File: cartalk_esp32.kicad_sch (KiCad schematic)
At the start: 24 parts, among them IC1 CP2104, J1 10118192-0002LF, Q1 mmbt2222, Q2 mmbt2222, SW2 KMR2, U1 HUB75 Connector Female, U2 AP2112-3.3, X2 ESP32_WROOM32_SKINNY

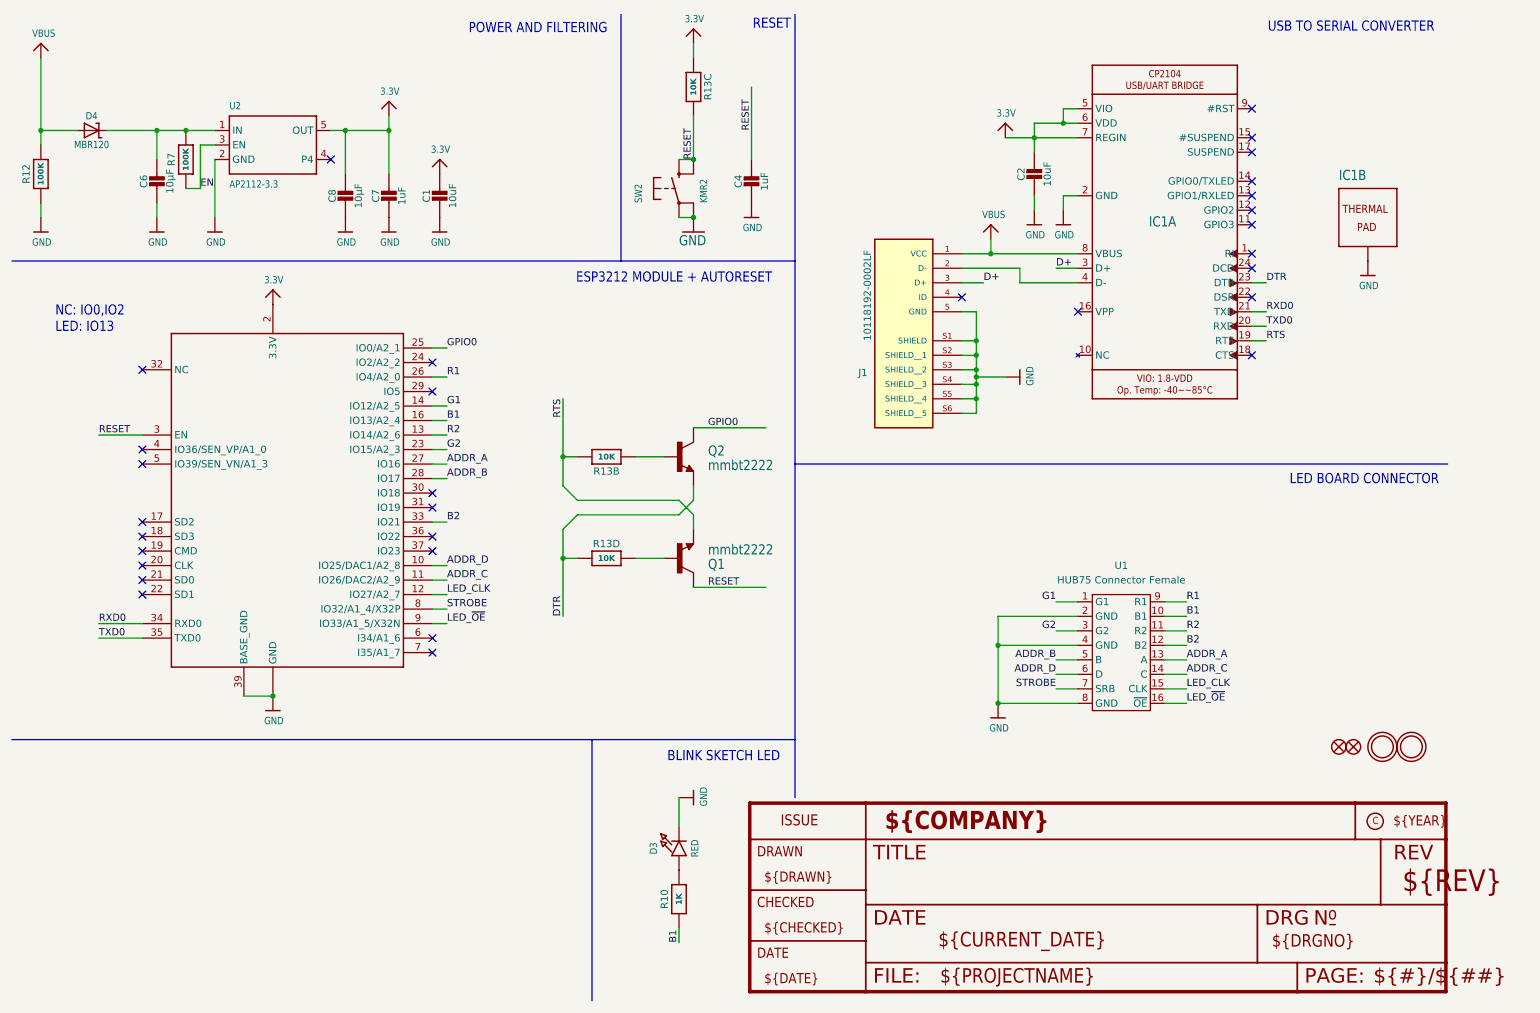
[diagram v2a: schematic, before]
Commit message: Fix remaining symbol-footprint pin mismatches.
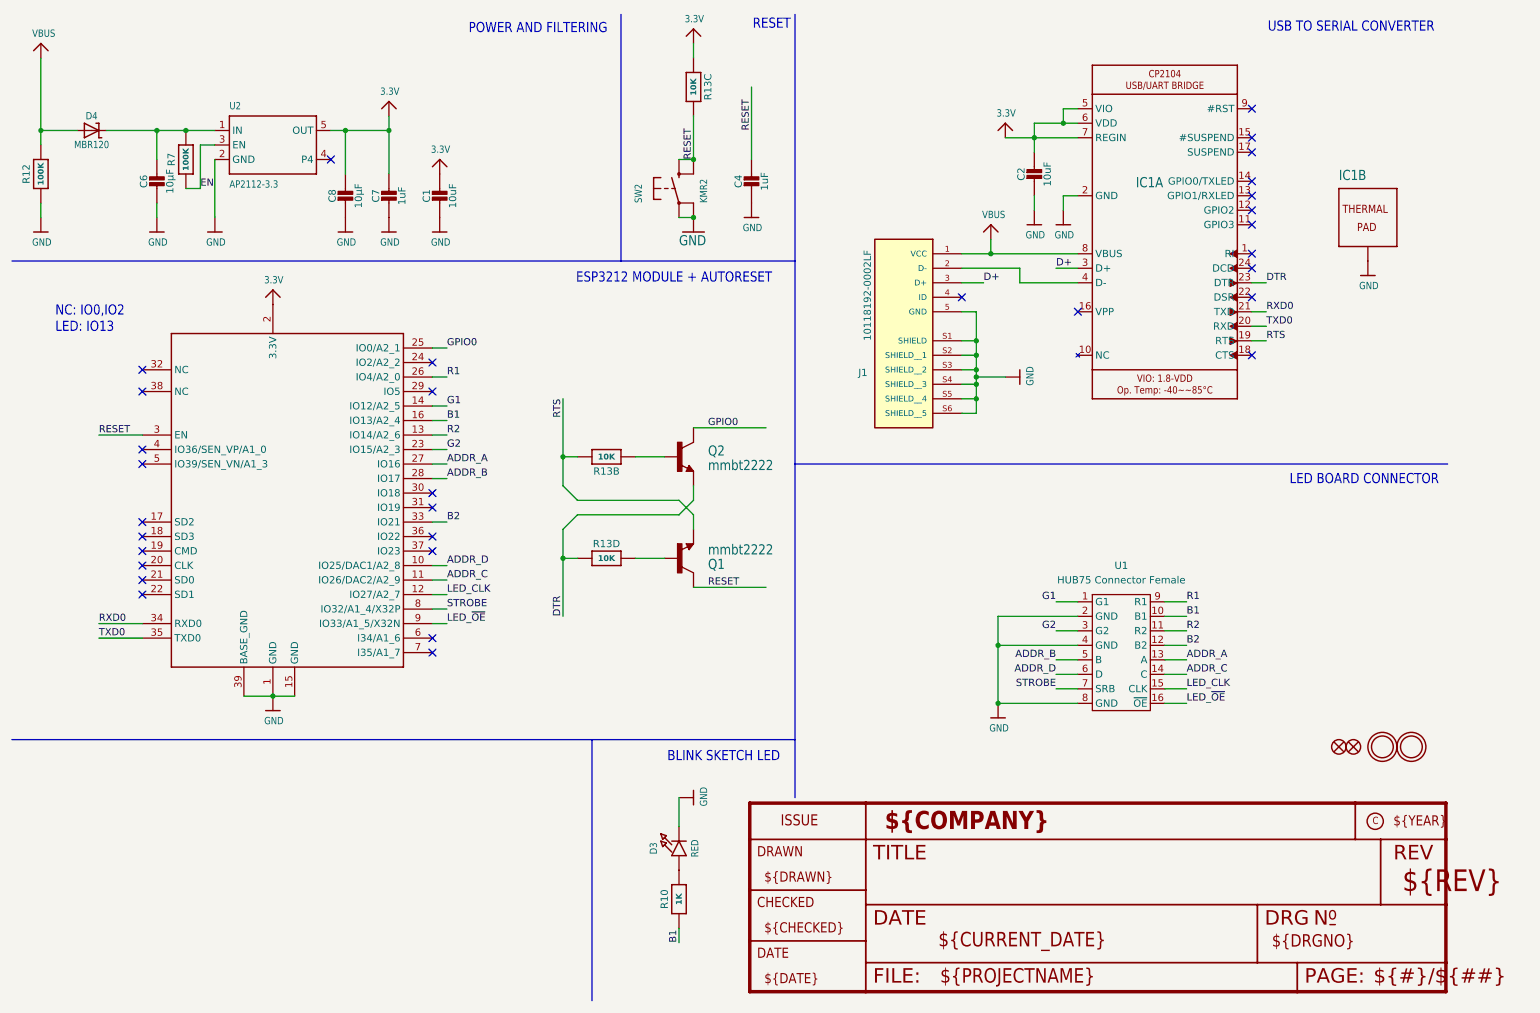
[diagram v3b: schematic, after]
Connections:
- net GND: now also D3.2 (C), IC1.25 (TP), SW2.1 (P), SW2.2 (P1); no longer D3.C, IC1.THERM (TP), SW2.A (P), SW2.A' (P1), X2.38 (GND), X2.P$1 (GND)
- net RESET: now also SW2.3 (S), SW2.4 (S1); no longer SW2.B (S), SW2.B' (S1)
- net VBUS: now also D4.1 (A); no longer D4.A
- net at C6.1, R7.2, U2.1 (IN): now also D4.2 (C); no longer D4.C
- net at R10.2: now also D3.1 (A); no longer D3.A
- no-connect marks 31 -> 32
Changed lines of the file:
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@@
 	)
 	(no_connect
+		(at 45.72 88.9)
+	)
+	(no_connect
 		(at 240.03 57.15)
 	)
@@
 		)
 	)
+	(wire
+		(pts
+			(xy 68.58 142.24) (xy 72.39 142.24)
+		)
+		(stroke
+			(width 0)
+			(type default)
+		)
+	)
 	(polyline
 		(pts
@@
 		(pin "9"
 		)
-		(pin "P$1"
-		)
 		(pin "18"
 		)
@@
 		(pin "37"
 		)
-		(pin "38"
-		)
 		(pin "4"
 		)
@@
 		(pin "14"
 		)
-		(pin "15"
-		)
 		(pin "16"
 		)
@@
 		(pin "32"
 		)
+		(pin "15"
+		)
+		(pin "38"
+		)
 		(instances
 			(project "cartalk_esp32"
@@
 	)
 	(symbol
+		(lib_name "CP2104_1")
 		(lib_id "cartalk_esp32-eagle-import:CP2104")
 		(at 224.79 59.69 0)
@@
 		(dnp no)
 		(property "Reference" "IC1"
-			(at 221.996 60.198 0)
+			(at 219.71 53.34 0)
 			(effects
 				(font
@@
 		(pin "9"
 		)
-		(pin "THERM"
+		(pin "25"
 		)
 		(instances
@@
 			)
 		)
-		(pin "C"
+		(pin "1"
 		)
-		(pin "A"
+		(pin "2"
 		)
 		(instances
@@
 		)
 		(property "Footprint" "smd_button:PTS645SL43SMTR92LFS_CNK-L"
-			(at 139.7 53.34 0)
+			(at 147.828 53.594 0)
 			(effects
 				(font
@@
 			)
 		)
-		(pin "A"
+		(pin "3"
 		)
-		(pin "A'"
+		(pin "2"
 		)
-		(pin "B"
+		(pin "4"
 		)
-		(pin "B'"
+		(pin "1"
 		)
 		(instances
@@
 		(pin "9"
 		)
-		(pin "THERM"
+		(pin "25"
 		)
 		(instances
@@
 			)
 		)
-		(pin "A"
+		(pin "1"
 		)
-		(pin "C"
+		(pin "2"
 		)
 		(instances

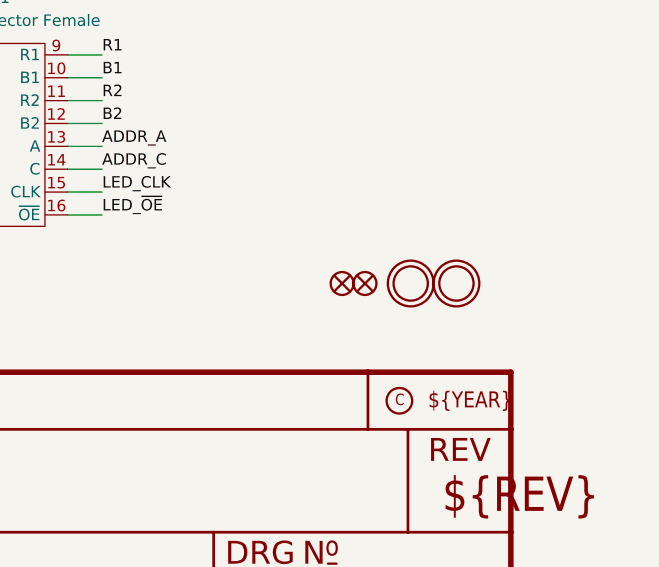
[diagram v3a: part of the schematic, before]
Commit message: Update component layout on board to fit in a small amount of space.
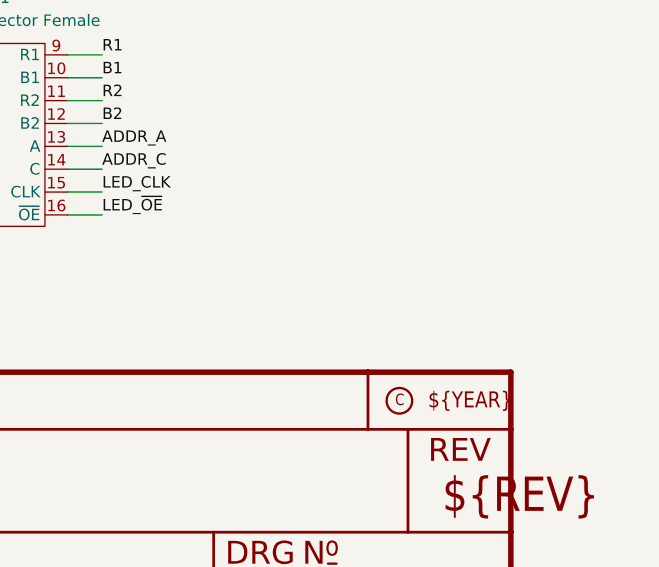
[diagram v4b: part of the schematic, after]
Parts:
- removed U$31, U$32: MOUNTINGHOLE2.5, MountingHole:MountingHole_2.5mm_Pad, symbol cartalk_esp32-eagle-import:MOUNTINGHOLE2.5
- removed U$34, U$35: FIDUCIAL_1MM, Fiducial:Fiducial_1mm_Mask2mm, symbol cartalk_esp32-eagle-import:FIDUCIAL_1MM
- D4: footprint Diode_SMD:D_SOD-123 -> cartalk_esp32:SOD-123
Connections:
- net VBUS: now also D4.2 (A); no longer D4.1 (A)
- net at C6.1, R7.2, U2.1 (IN): now also D4.1 (C); no longer D4.2 (C)

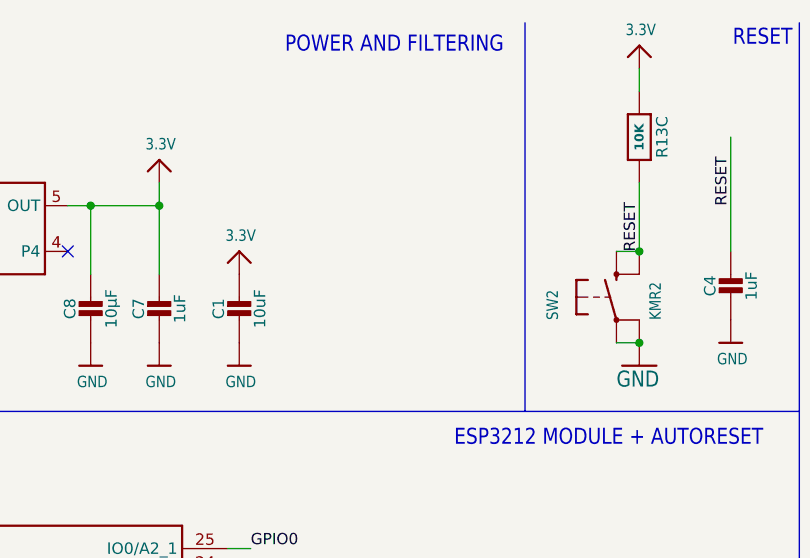
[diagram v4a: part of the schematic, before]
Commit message: Add power pads for soldering on 5V.
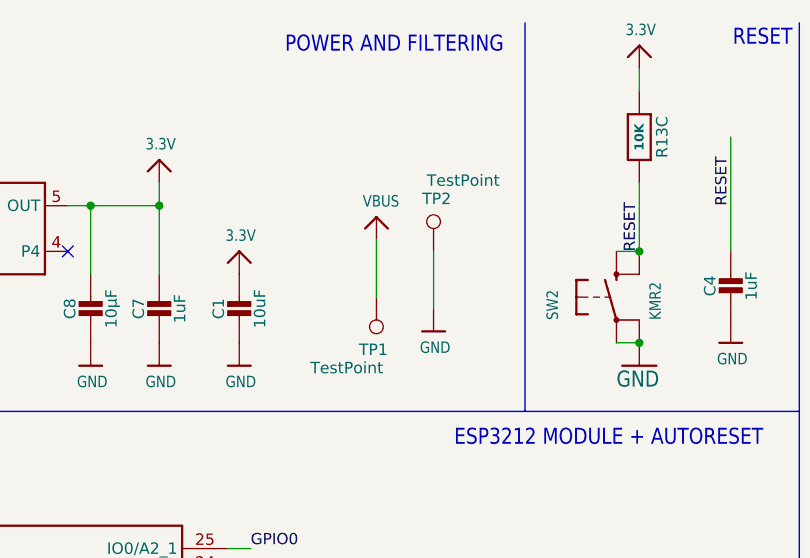
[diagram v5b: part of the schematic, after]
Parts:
- added TP1, TP2: TestPoint, TestPoint:TestPoint_THTPad_D3.0mm_Drill1.5mm, symbol Connector:TestPoint
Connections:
- net GND: now also TP2.1
- net VBUS: now also TP1.1

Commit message: Handle some DRC errors.
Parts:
- D4: footprint cartalk_esp32:SOD-123 -> Diode_SMD:D_SOD-123
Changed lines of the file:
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@@
 			)
 		)
-		(property "Footprint" "cartalk_esp32:SOD-123"
+		(property "Footprint" "Diode_SMD:D_SOD-123"
 			(at 37.592 38.608 0)
 			(effects

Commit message: Swap silkscreen labels of D3 and R12 where they should be.
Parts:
- C1, C2: value 10uF -> 10µF
- C4, C7: value 1uF -> 1µF
- C8: footprint Capacitor_SMD:C_0805_2012Metric_Pad1.18x1.45mm_HandSolder -> Capacitor_SMD:C_0805_2012Metric
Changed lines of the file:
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@@
 			)
 		)
-		(property "Value" "10uF"
+		(property "Value" "10µF"
 			(at 100.09 54.63 90)
 			(effects
@@
 			)
 		)
-		(property "Value" "1uF"
+		(property "Value" "1µF"
 			(at 91.2 54.63 90)
 			(effects
@@
 			)
 		)
-		(property "Value" "10uF"
+		(property "Value" "10µF"
 			(at 204.23 50.82 90)
 			(effects
@@
 			)
 		)
-		(property "Value" "1uF"
+		(property "Value" "1µF"
 			(at 154.7 52.09 90)
 			(effects
@@
 			)
 		)
-		(property "Footprint" "Capacitor_SMD:C_0805_2012Metric_Pad1.18x1.45mm_HandSolder"
+		(property "Footprint" "Capacitor_SMD:C_0805_2012Metric"
 			(at 81.28 55.88 0)
 			(effects
